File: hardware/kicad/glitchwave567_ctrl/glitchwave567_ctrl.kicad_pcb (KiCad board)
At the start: 2 copper layers, 0 parts

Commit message: hardware: LAYOUT phase 1 - both boards placed via pcbnew API (296+22 footprints, nets bound)
pcbgen.py: netlist-driven board authoring (pcbnew python 7.0.11) - footprint
instantiation with per-pad net binding, corner-notched outline, spiral
auto-placement of passives near net-neighbor anchors (pad-extent collision),
GND zones both layers staged. Wall jacks auto-oriented; audit confirms zero
pads outside outline. Audio chain right-to-left (IN->dirt->567->SVF->OUT),
buck top-center, Pico+digital bottom, ctrl board pots 3+3 grid at drill
positions, header at identical enclosure XY on both boards (stack mates).
Routing (custom grid A*) next.

Co-Authored-By: Claude Fable 5 <noreply@anthropic.com>
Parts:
- added C1: 100n, C_0603_1608Metric, F.Cu at (69.8, 60.0)
- added C2: 100n, C_0603_1608Metric, F.Cu at (69.4, 62.4)
- added C3: 100n, C_0603_1608Metric, F.Cu at (65.8, 60.0)
- added C4: 100n, C_0603_1608Metric, F.Cu at (73.8, 60.0)
- added C5: 100n, C_0603_1608Metric, F.Cu at (70.2, 64.7)
- added C6: 100n, C_0603_1608Metric, F.Cu at (65.7, 63.5)
- added C7: 100u, CP_Elec_6.3x7.7, F.Cu at (122.0, 76.0)
- added J1: to MAIN 2x8, PinHeader_2x08_P2.54mm_Vertical, F.Cu at (96.0, 104.0)
- added LED1: WS2812B, LED_WS2812B_PLCC4_5.0x5.0mm_P3.2mm, F.Cu at (34.0, 36.0)
- added LED2: WS2812B, LED_WS2812B_PLCC4_5.0x5.0mm_P3.2mm, F.Cu at (69.0, 36.0)
- added LED3: WS2812B, LED_WS2812B_PLCC4_5.0x5.0mm_P3.2mm, F.Cu at (104.0, 36.0)
- added LED4: WS2812B, LED_WS2812B_PLCC4_5.0x5.0mm_P3.2mm, F.Cu at (34.0, 76.0)
- added LED5: WS2812B, LED_WS2812B_PLCC4_5.0x5.0mm_P3.2mm, F.Cu at (104.0, 76.0)
- added LED6: WS2812B, LED_WS2812B_PLCC4_5.0x5.0mm_P3.2mm, F.Cu at (69.0, 76.0)
- added RV1: B10k (FREQ), ALPS_RK09K1130, F.Cu at (34.0, 22.0)
- added RV2: B10k (GAIN), ALPS_RK09K1130, F.Cu at (69.0, 22.0)
- added RV3: B10k (MIX), ALPS_RK09K1130, F.Cu at (104.0, 22.0)
- added RV4: B10k (FIZZ), ALPS_RK09K1130, F.Cu at (34.0, 50.0)
- added RV5: B10k (Q), ALPS_RK09K1130, F.Cu at (69.0, 50.0)
- added RV6: B10k (VOL), ALPS_RK09K1130, F.Cu at (104.0, 50.0)
- added SW1: Suntsu SSWFS-S01 (TAP/BYP), SSWFS-S01, F.Cu at (34.0, 96.0)
- added SW2: Suntsu SSWFS-S01 (TAP/BYP), SSWFS-S01, F.Cu at (104.0, 96.0)
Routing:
- added copper zone on B.Cu, net GND
- added copper zone on F.Cu, net GND
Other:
- board outline added: 138 x 114 mm
- board text added: "BYPASS"
- board text added: "FIZZ Q VOL"
- board text added: "FREQ GAIN MIX"
- board text added: "GLITCHWAVE 567 - CONTROL rev0.1 Illicit Apothecary"
- board text added: "TAP"

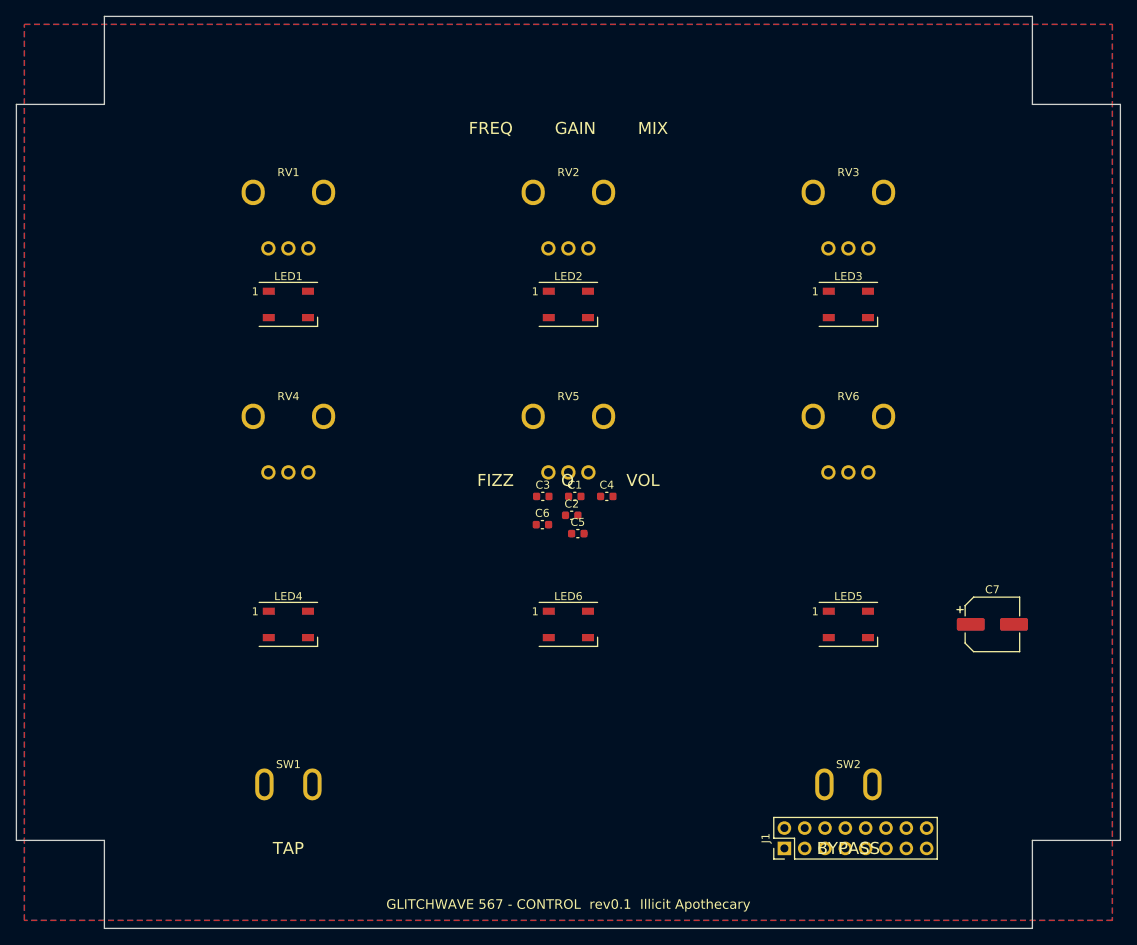
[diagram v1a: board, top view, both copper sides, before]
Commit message: hardware: ROUTING complete (0 unrouted nets both boards) via custom grid A* - DRC punch list captured
router.py: 0.508mm grid A*, F.Cu-horizontal/B.Cu-vertical bias, 45deg moves,
via cost, pad-escape cells, rotation-aware pad claims, same-net adjacent-pin
preroute w/ union-join, best-of-N orderings + priority retry. MAIN 210 nets
routed after placement fixes (env chain + U17 relocated from walled pocket);
CTRL 16 nets. GND pours filled + stitching vias.
KNOWN DRC punch list (KiCad 10): diagonal track crossings (need corner-cut
rule), preroute segments crossing intermediate pads (need corridor check),
hole clearance margin, starved thermals -> solid pad connection, 98
unconnected (drc_main.json has items). Fix round next.

Co-Authored-By: Claude Fable 5 <noreply@anthropic.com>
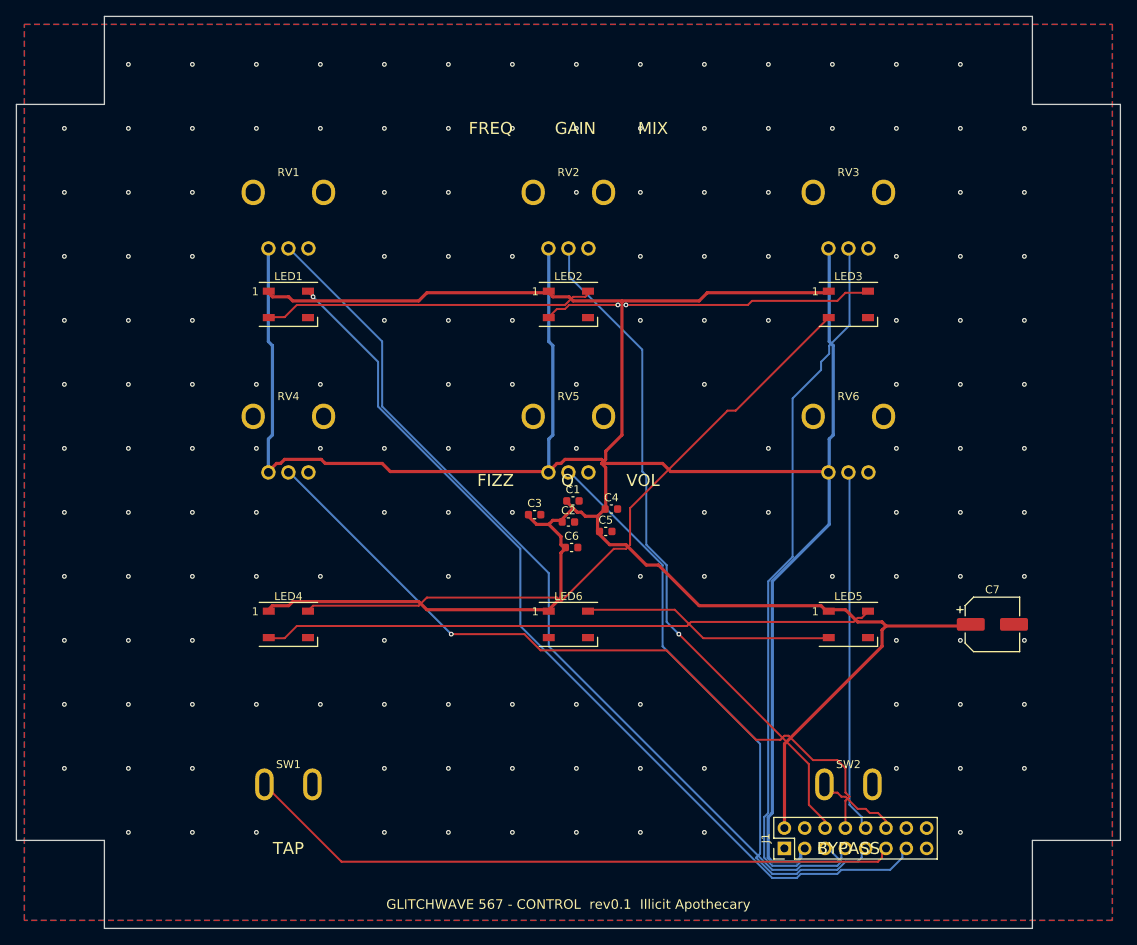
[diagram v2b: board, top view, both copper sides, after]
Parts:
- moved C6 4.64 mm to (69.4, 66.4)
- moved C5 3.50 mm to (73.7, 64.4)
- moved C3 2.50 mm to (64.8, 62.3)
- moved C4 1.68 mm to (74.4, 61.6)
- moved C2 0.93 mm to (69.0, 63.2)
- moved C1 0.61 mm to (69.6, 60.6)
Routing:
- net +5V: track 0.00 -> 244.7 mm
- net 3V3: track 0.00 -> 214.8 mm
- net /WS_IN: track 0.00 -> 115.7 mm, vias 0 -> 1
- net /POT1_W: track 0.00 -> 114.5 mm
- net /POT4_W: track 0.00 -> 93.4 mm, vias 0 -> 1
- net /POT3_W: track 0.00 -> 92.3 mm
- net /POT2_W: track 0.00 -> 85.9 mm, vias 0 -> 1
- net /WSD3: track 0.00 -> 83.3 mm
- net /STOMP1: track 0.00 -> 82.7 mm
- net /WSD4: track 0.00 -> 76.7 mm
- net /POT5_W: track 0.00 -> 74.5 mm
- net /POT6_W: track 0.00 -> 45.5 mm
- net /WSD2: track 0.00 -> 41.4 mm, vias 0 -> 2
- net /WSD1: track 0.00 -> 41.4 mm
- net /WSD5: track 0.00 -> 31.4 mm
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
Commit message: hardware: router physics tuned (grid 0.55 + diagonals + pad-graze guard + 0.13mm design rules); ctrl 100% routed, main ~195/210; 3D renders
Co-Authored-By: Claude Fable 5 <noreply@anthropic.com>
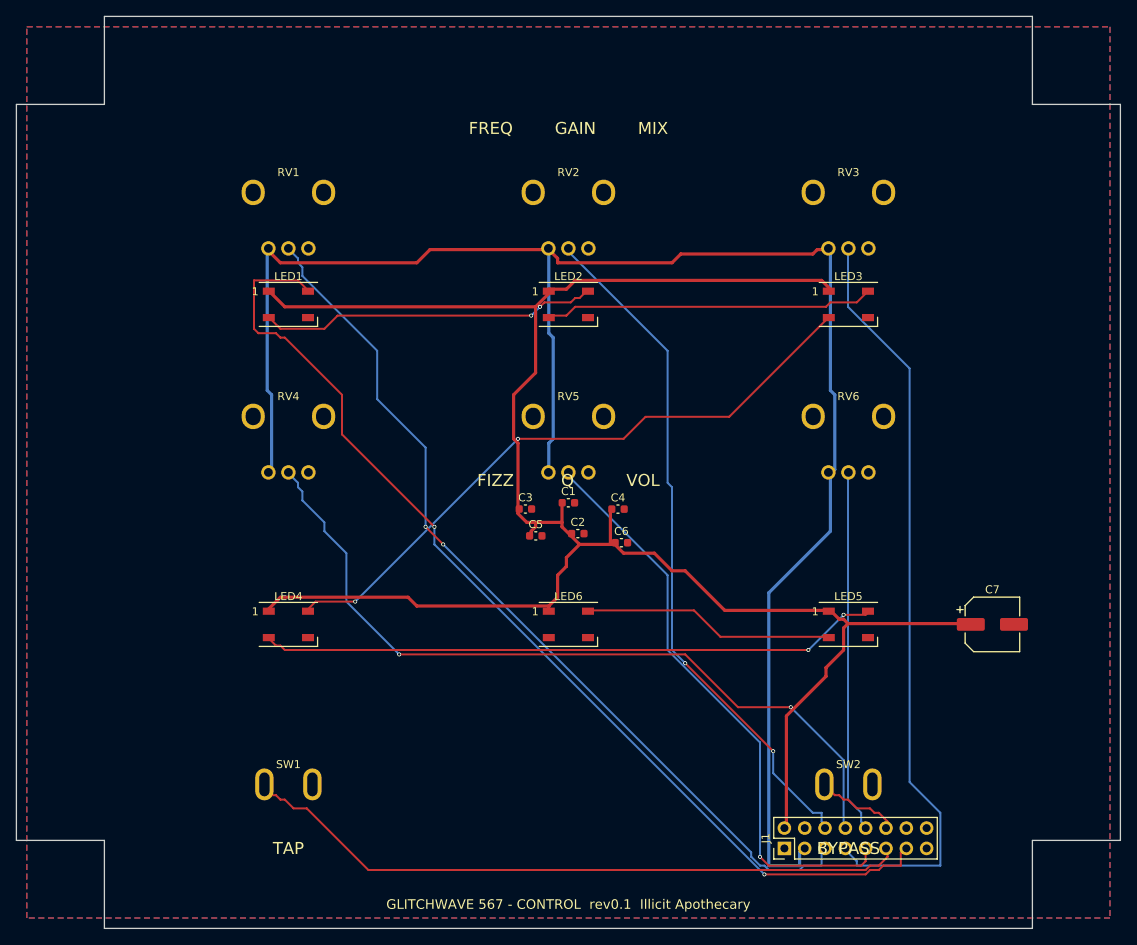
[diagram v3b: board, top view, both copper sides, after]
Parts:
- moved C5 8.76 mm to (64.9, 64.9)
- moved C6 6.25 mm to (75.6, 65.8)
- moved C2 1.87 mm to (70.2, 64.7)
- moved C3 1.35 mm to (63.6, 61.6)
- moved C4 0.83 mm to (75.2, 61.6)
- moved C1 0.61 mm to (69.0, 60.8)
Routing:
- net /WS_IN: track 115.7 -> 129.3 mm, vias 1 -> 2
- net /POT4_W: track 93.4 -> 97.5 mm, vias 1 -> 2
- net /POT3_W: track 92.3 -> 95.1 mm
- net /WSD3: track 83.3 -> 80.7 mm, vias 0 -> 2
- net 3V3: track 214.8 -> 217.4 mm
- net /POT1_W: track 114.5 -> 112.0 mm, vias 0 -> 2
- net +5V: track 244.7 -> 246.5 mm
- net /STOMP1: track 82.7 -> 84.2 mm
- net /WSD1: track 41.4 -> 42.9 mm, vias 0 -> 2
- net /WSD4: track 76.7 -> 78.1 mm, vias 0 -> 2
- net /POT5_W: track 74.5 -> 73.4 mm, vias 0 -> 1
- net /POT6_W: track 45.5 -> 44.9 mm
- net /POT2_W: track 85.9 -> 86.1 mm, vias 1 -> 2
- net /WSD2: track 41.4 -> 41.5 mm, vias 2 -> 0
- net GND: vias 156 -> 0

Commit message: hardware: 4-LAYER pivot + width-aware router - ctrl board DONE (routed, 0 unconnected, 22 DRC), main 3 airwires left
Moved to 4-layer (In1=GND plane, In2=routing) after proving 2-layer congestion
was structural - PCBWay ~+20USD, better audio grounding. Router: via-in-own-pad
escapes (the breakthrough: 0 fails in 32s pre-guards), rip-up/reroute with
power-net protection + best-state checkpointing, width-aware rules (power
rectilinear, full via cross-guard), notch keepouts in placer (R93 was IN the
notch), GND via per SMD ground pad. Main board: 207/210 nets, 3 airwires
(TRIM_FA/LAD_OUT/SVF_SUM) for the polish round.

Co-Authored-By: Claude Fable 5 <noreply@anthropic.com>
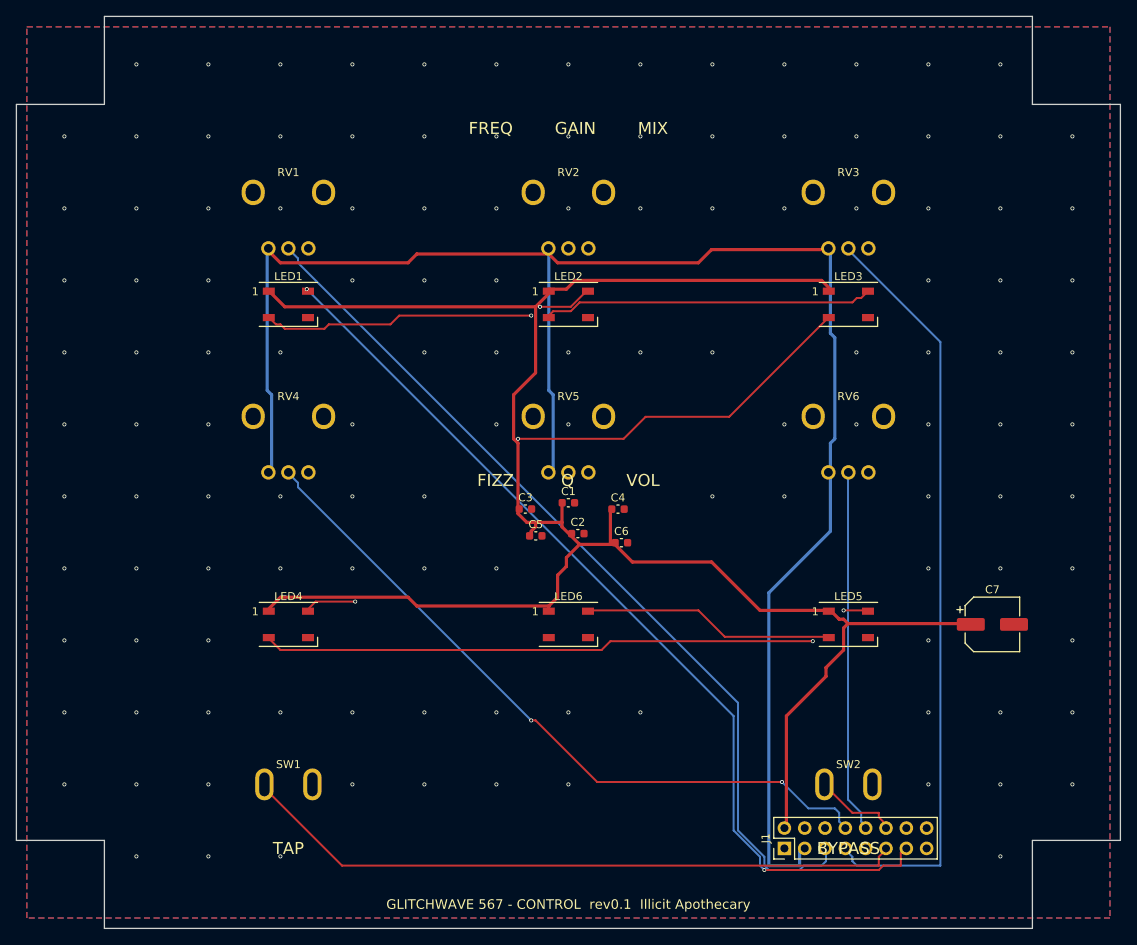
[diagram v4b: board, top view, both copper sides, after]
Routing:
- net /WS_IN: track 129.3 -> 116.0 mm
- net /POT4_W: track 97.5 -> 88.5 mm
- net /POT1_W: track 112.0 -> 111.6 mm, vias 2 -> 0
- net /POT2_W: vias 2 -> 0
- net GND: vias 0 -> 128
- net /POT5_W: vias 1 -> 0
- added copper zone on In1.Cu, net GND
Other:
- copper layers 2 -> 4
